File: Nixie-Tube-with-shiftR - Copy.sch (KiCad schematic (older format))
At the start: 56 parts, among them J1 Conn_01x06_Male, J2 HV_IN, J3 Conn_01x06_Female, J4 HV_OUT, Q1 MMBTA42LT1, Q10 MMBTA42LT1, Q11 AO3400, Q12 AO3400, Q13 AO3400, Q14 MMBTA42LT1, Q15 MMBTA42LT1, Q2 MMBTA42LT1, Q3 MMBTA42LT1, Q4 MMBTA42LT1, Q5 MMBTA42LT1, Q6 MMBTA42LT1, Q7 MMBTA42LT1, Q8 MMBTA42LT1, Q9 MMBTA42LT1, U1 74HC595D, U3 74HC595D, U4 ams1117-5.0

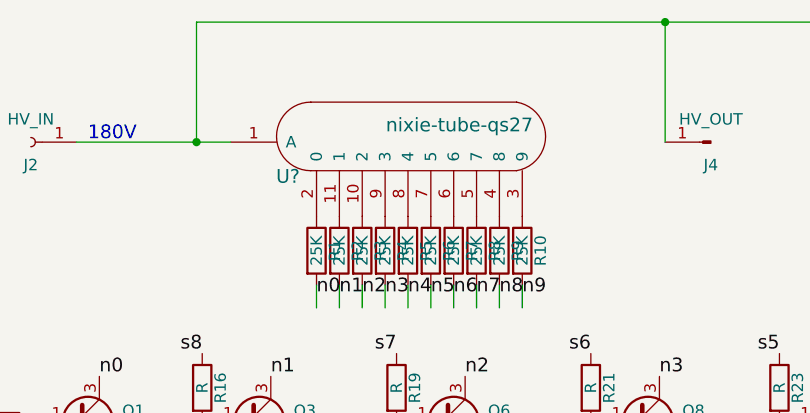
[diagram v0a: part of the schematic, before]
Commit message: routed qs27-1 on the main pcbnew
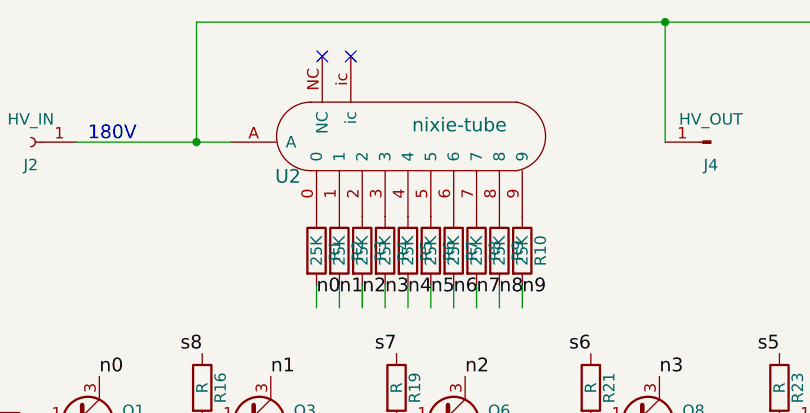
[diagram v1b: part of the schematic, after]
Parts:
- removed U?: nixie-tube-qs27, nixie-tube-fp:qs27-1, symbol nixie-tube-qs27
- added U2: nixie-tube, nixie-tube-fp:qs30-1, symbol nixie-tube
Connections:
- no-connect marks 1 -> 3
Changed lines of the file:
@@
 Text Label 6225 4250 1    60   ~ 0
 DotD
+$Comp
+L nixie-tube U2
+U 1 1 59E3559F
+P 5450 1950
+F 0 "U2" H 4875 2050 60  0000 C CNN
+F 1 "nixie-tube" H 5625 2275 60  0000 C CNN
+F 2 "nixie-tube-fp:qs30-1" H 5150 1975 60  0001 C CNN
+F 3 "" H 5150 1975 60  0001 C CNN
+	1    5450 1950
+	1    0    0    -1
+$EndComp
+NoConn ~ 5025 1325
+NoConn ~ 5150 1325
 Wire Wire Line
 	2050 3750 3325 3750
@@
 	1    0    0    -1
 $EndComp
-$Comp
-L nixie-tube-qs27 U?
-U 1 1 5A0C1069
-P 5450 1950
-F 0 "U?" H 4875 2050 60  0000 C CNN
-F 1 "nixie-tube-qs27" H 5625 2275 60  0000 C CNN
-F 2 "nixie-tube-fp:qs27-1" H 5150 1975 60  0001 C CNN
-F 3 "" H 5150 1975 60  0001 C CNN
-	1    5450 1950
-	1    0    0    -1
-$EndComp
